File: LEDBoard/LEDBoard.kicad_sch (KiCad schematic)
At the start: 17 parts, among them J1 X0511FVS-24AS-LPV01, J2 X0511FVS-24AS-LPV01, Q1 AO3401A, SW1 SKRTLA

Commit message: Minor board updates
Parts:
- added C2: 1uF, Capacitor_SMD:C_0402_1005Metric, symbol Device:C_Small
- added C3: 10uF, Capacitor_SMD:C_0603_1608Metric, symbol Device:C_Small
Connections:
- net -BATT: now also C2.2, C3.2
- net BATT_TERM: now also C2.1, C3.1
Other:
- moved on the sheet: BT1, C1, D1, D2, D3, D4, J1, J2, Q1, R1, R2, R3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

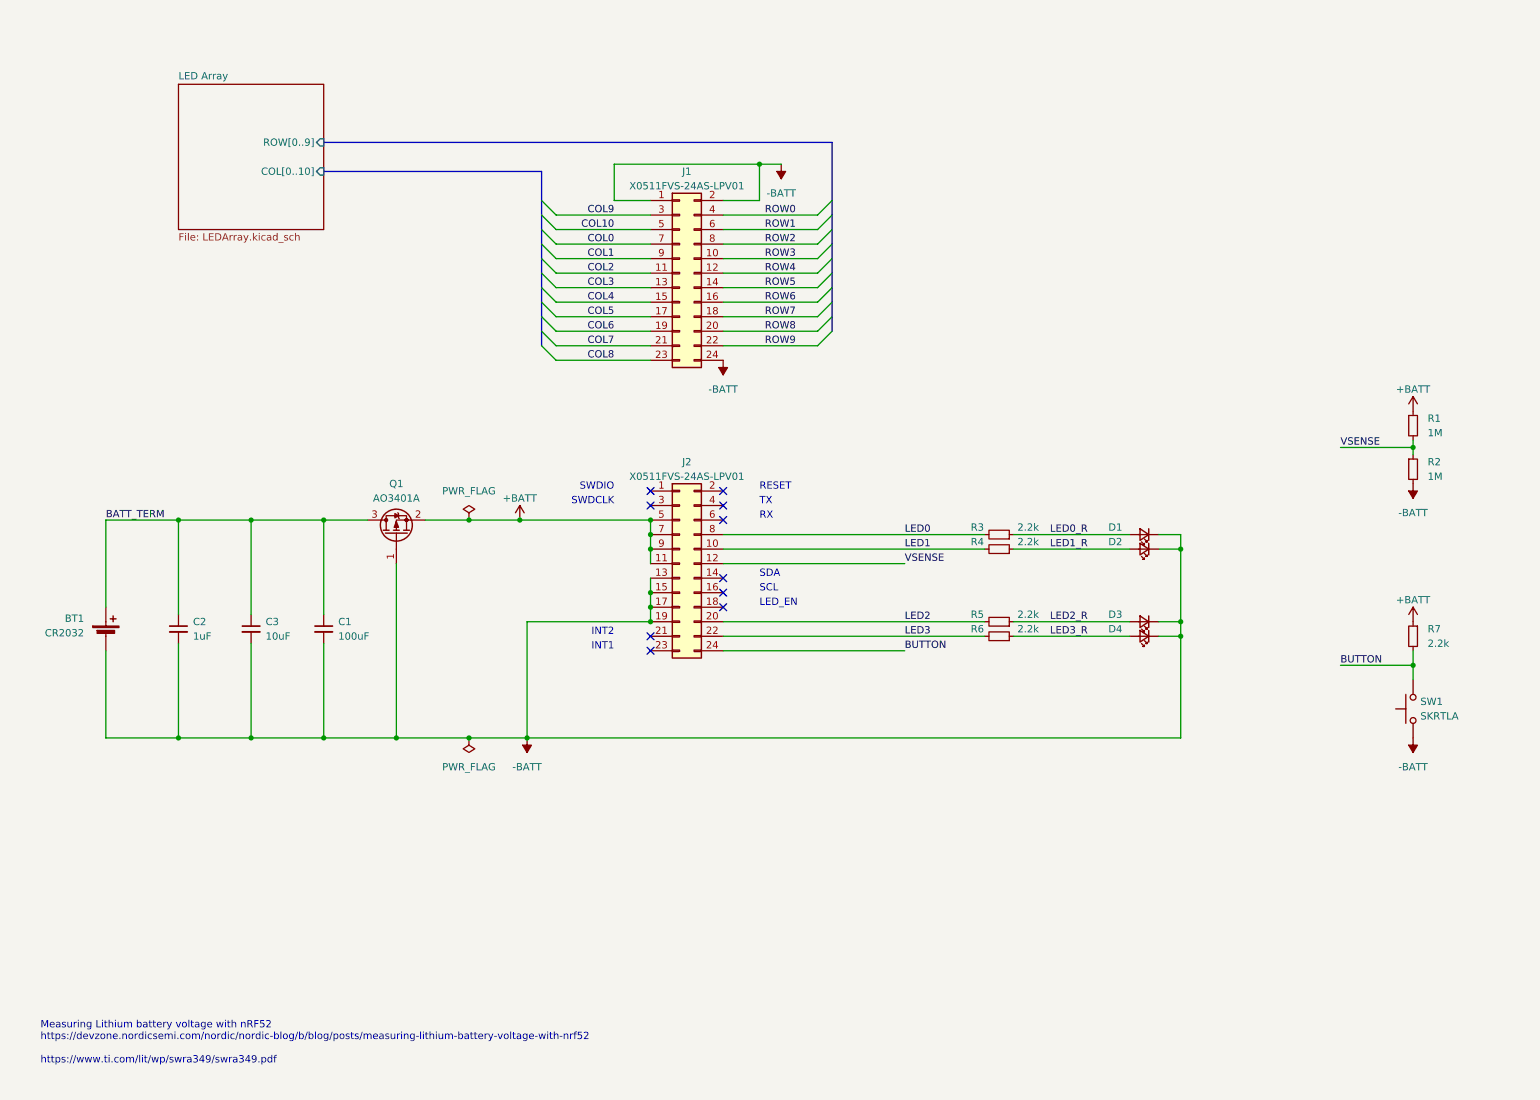
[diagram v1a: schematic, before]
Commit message: Remove LED driver
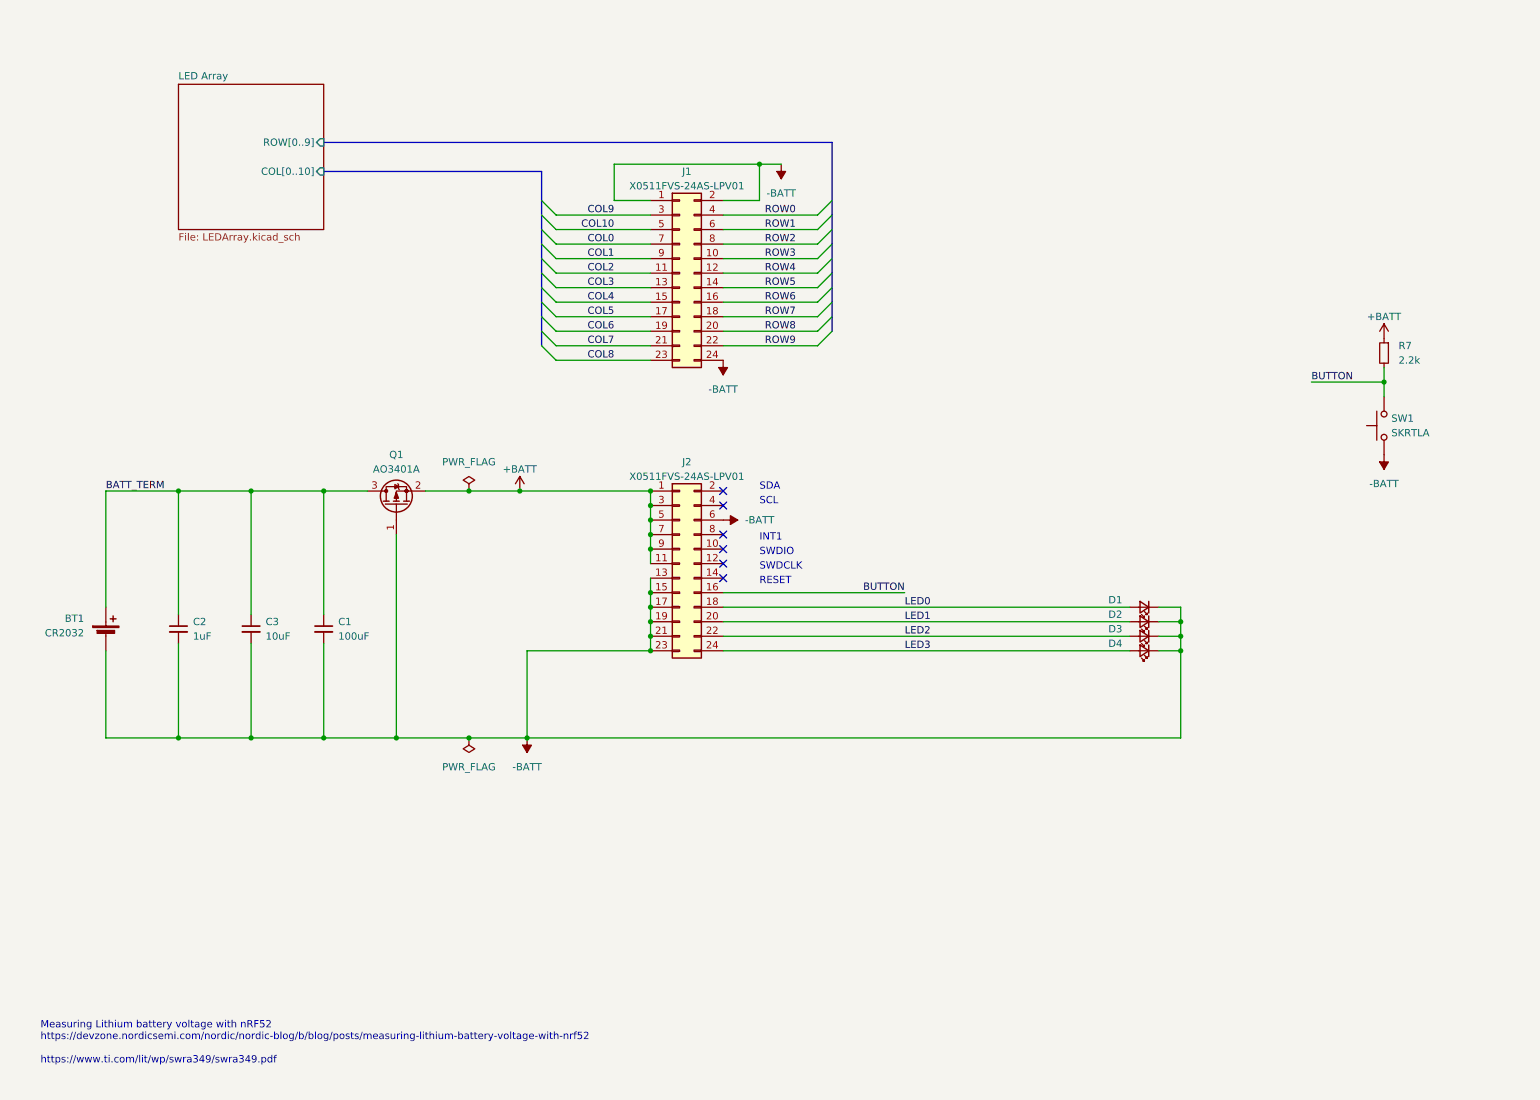
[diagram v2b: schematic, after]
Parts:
- removed R1, R2: 1M, Resistor_SMD:R_0402_1005Metric, symbol Device:R_Small
- removed R3, R4, R5, R6: 2.2k, Resistor_SMD:R_0402_1005Metric, symbol Device:R_Small
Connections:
- net LED0_R is gone; now on net LED0: D1.2 (A)
- net LED1_R is gone; now on net LED1: D2.2 (A)
- net LED2_R is gone; now on net LED2: D3.2 (A)
- net LED3_R is gone; now on net LED3: D4.2 (A)
- net +BATT: now also J2.1 (Pin_1), J2.3 (Pin_3)
- net -BATT: now also J2.21 (Pin_21), J2.23 (Pin_23), J2.6 (Pin_6)
- net BUTTON: now also J2.16 (Pin_16); no longer J2.24 (Pin_24)
- net LED0: now also J2.18 (Pin_18); no longer J2.8 (Pin_8)
- net LED1: now also J2.20 (Pin_20); no longer J2.10 (Pin_10)
- net LED2: now also J2.22 (Pin_22); no longer J2.20 (Pin_20)
- net LED3: now also J2.24 (Pin_24); no longer J2.22 (Pin_22)
- net VSENSE: no longer names the net of J2.12 (Pin_12)
- no-connect marks 10 -> 6
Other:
- note removed: "INT2"
- note removed: "LED_EN"
- note removed: "RX"
- note removed: "TX"
- moved on the sheet: D1, D2, D3, D4, Q1, R7, SW1

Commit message: Change led matrix routing for sinking current through mcu, sourcing from battery
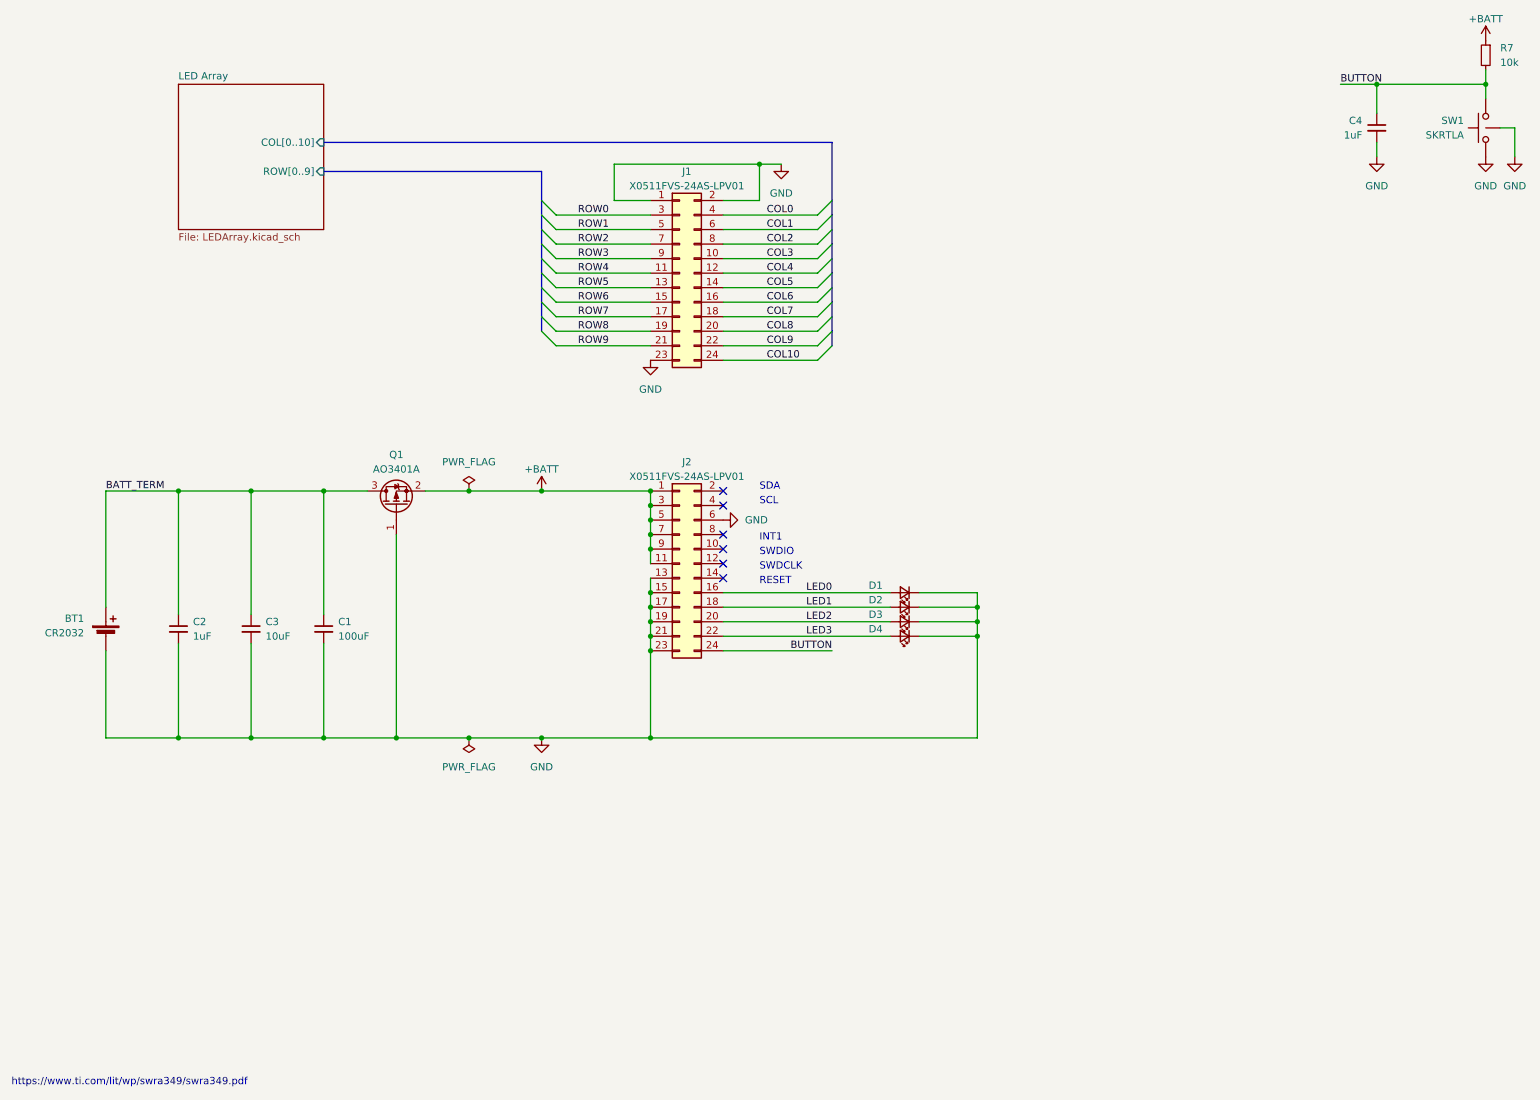
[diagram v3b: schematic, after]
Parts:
- removed SW1: SKRTLA, Button_Switch_SMD:SW_Push_1P1T-MP_NO_Horizontal_Alps_SKRTLAE010, symbol Switch:SW_Push
- added C4: 1uF, Capacitor_SMD:C_0402_1005Metric, symbol Device:C_Small
- added SW1: SKRTLA, Button_Switch_SMD:SW_Push_1P1T-MP_NO_Horizontal_Alps_SKRTLAE010, symbol WordWatch:SW_Push_MP
- R7: value 2.2k -> 10k
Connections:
- net BUTTON: now also J2.24 (Pin_24), C4.1, SW1.2; no longer J2.16 (Pin_16)
- net COL0: now also J1.4 (Pin_4); no longer J1.7 (Pin_7)
- net COL1: now also J1.6 (Pin_6); no longer J1.9 (Pin_9)
- net COL10: now also J1.24 (Pin_24); no longer J1.5 (Pin_5)
- net COL2: now also J1.8 (Pin_8); no longer J1.11 (Pin_11)
- net COL3: now also J1.10 (Pin_10); no longer J1.13 (Pin_13)
- net COL4: now also J1.12 (Pin_12); no longer J1.15 (Pin_15)
- net COL5: now also J1.14 (Pin_14); no longer J1.17 (Pin_17)
- net COL6: now also J1.16 (Pin_16); no longer J1.19 (Pin_19)
- net COL7: now also J1.18 (Pin_18); no longer J1.21 (Pin_21)
- net COL8: now also J1.20 (Pin_20); no longer J1.23 (Pin_23)
- net COL9: now also J1.22 (Pin_22); no longer J1.3 (Pin_3)
- net LED0: now also J2.16 (Pin_16); no longer J2.18 (Pin_18)
- net LED1: now also J2.18 (Pin_18); no longer J2.20 (Pin_20)
- net LED2: now also J2.20 (Pin_20); no longer J2.22 (Pin_22)
- net LED3: now also J2.22 (Pin_22); no longer J2.24 (Pin_24)
- net ROW0: now also J1.3 (Pin_3); no longer J1.4 (Pin_4)
- net ROW1: now also J1.5 (Pin_5); no longer J1.6 (Pin_6)
- net ROW2: now also J1.7 (Pin_7); no longer J1.8 (Pin_8)
- net ROW3: now also J1.9 (Pin_9); no longer J1.10 (Pin_10)
- net ROW4: now also J1.11 (Pin_11); no longer J1.12 (Pin_12)
- net ROW5: now also J1.13 (Pin_13); no longer J1.14 (Pin_14)
- net ROW6: now also J1.15 (Pin_15); no longer J1.16 (Pin_16)
- net ROW7: now also J1.17 (Pin_17); no longer J1.18 (Pin_18)
- net ROW8: now also J1.19 (Pin_19); no longer J1.20 (Pin_20)
- net ROW9: now also J1.21 (Pin_21); no longer J1.22 (Pin_22)
- net -BATT renamed GND
- net GND: now also J1.23 (Pin_23), C4.2, SW1.1, SW1.MP; no longer J1.24 (Pin_24)
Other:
- note added: "https://www.ti.com/lit/wp/swra349/swra349.pdf"
- note removed: "Measuring Lithium battery voltage with nRF52 https://devzone.nordicsemi.com/nordic/nordic-blog/b/blog/posts/measuring-lithium-battery-voltage-with-nrf52 https://www.ti.com/lit/wp/swra349/swra349.pdf"
- title: (none) -> WordWatch - LED Board
- moved on the sheet: D1, D2, D3, D4, R7
